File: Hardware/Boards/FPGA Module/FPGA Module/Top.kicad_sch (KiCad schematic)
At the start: 0 parts

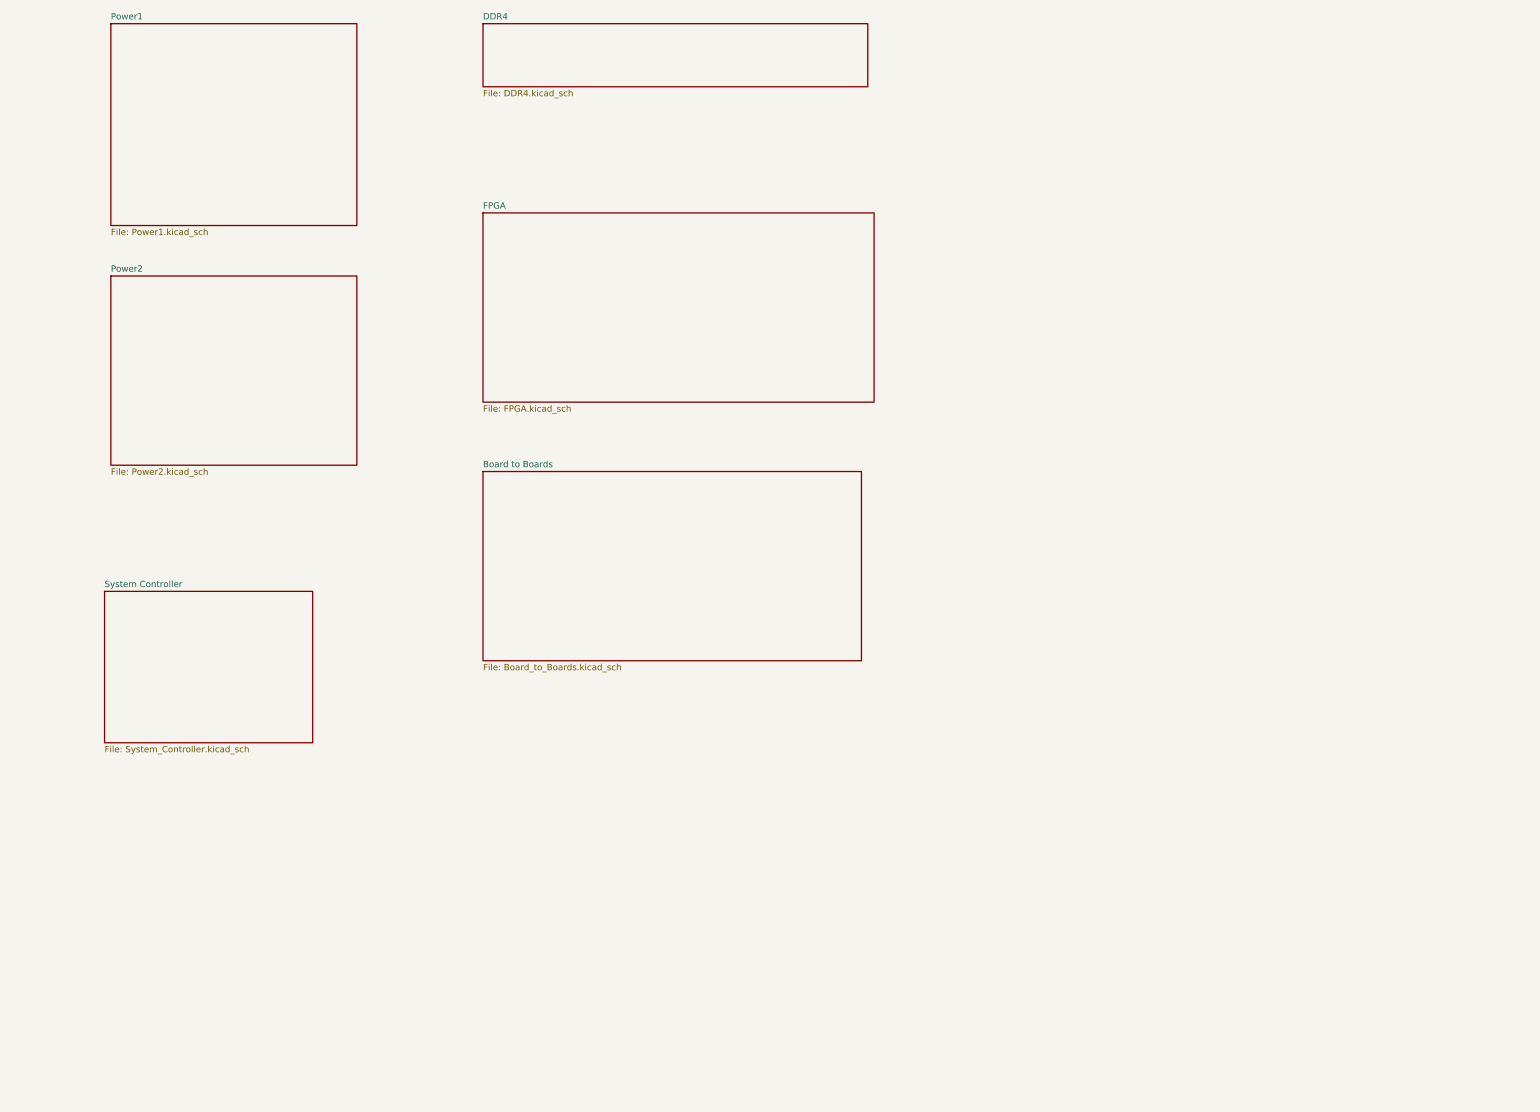
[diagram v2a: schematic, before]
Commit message: FPGA Module schematic and part edits
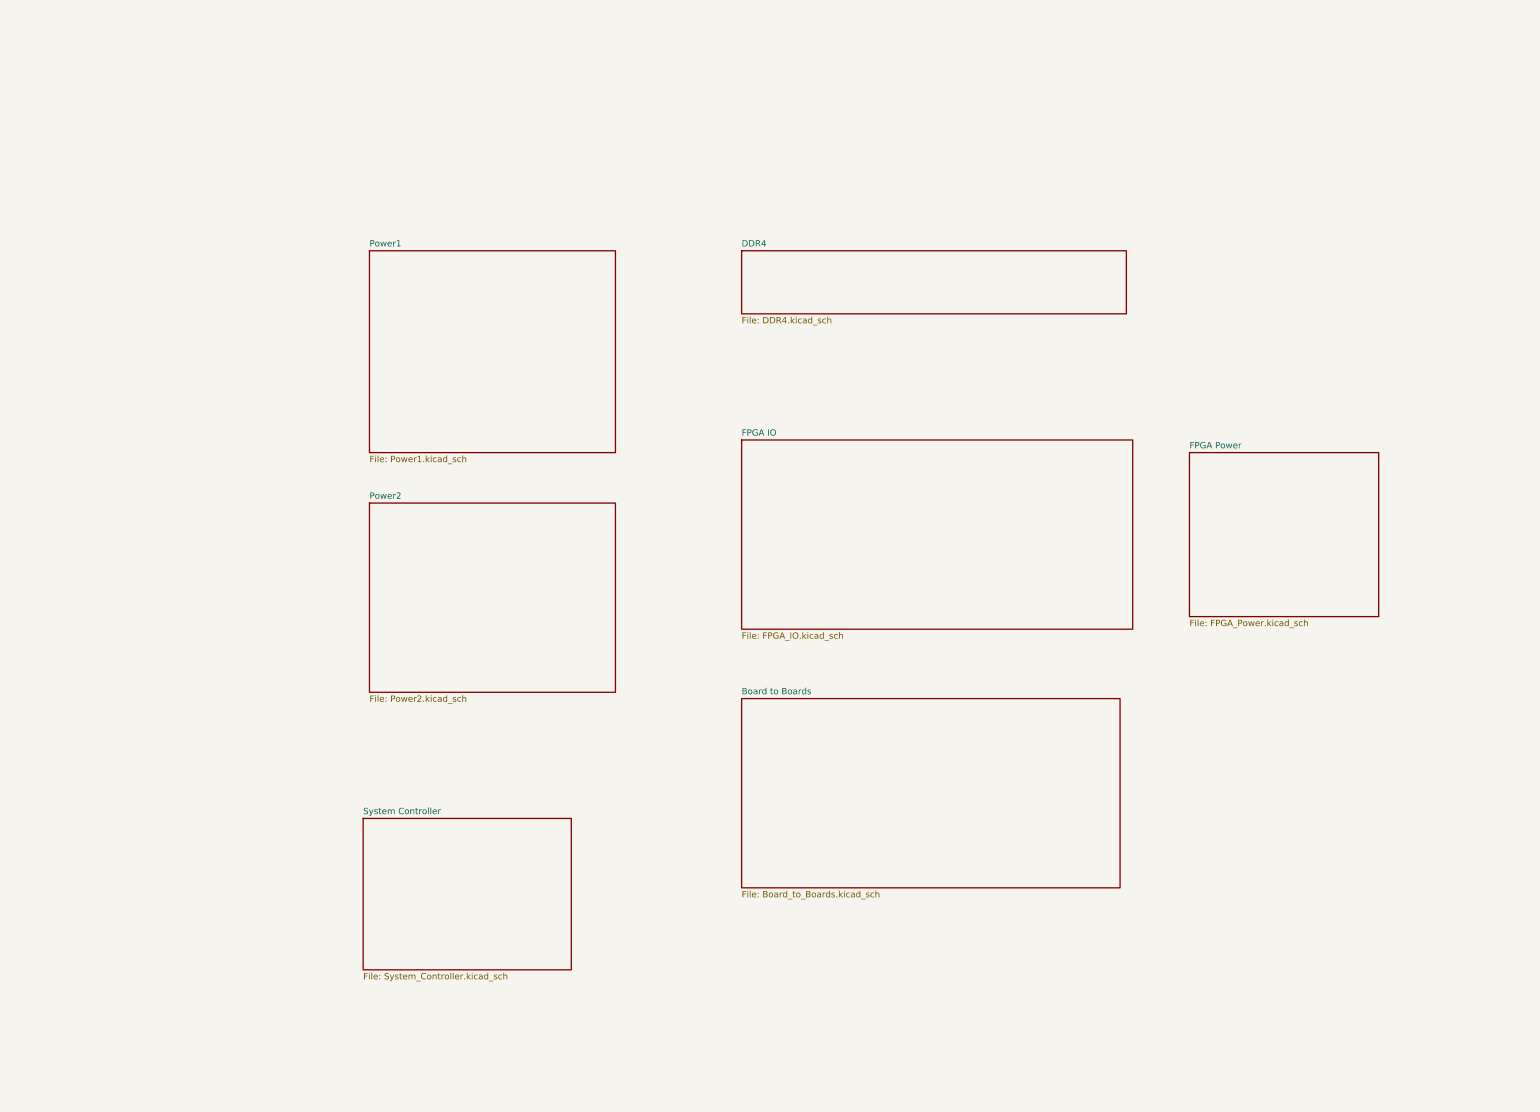
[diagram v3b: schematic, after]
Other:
- sheet FPGA renamed FPGA IO
- added sheet FPGA Power (FPGA_Power.kicad_sch)
- sheet FPGA IO: file FPGA.kicad_sch -> FPGA_IO.kicad_sch
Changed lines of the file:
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@@
 	(generator "eeschema")
 	(generator_version "8.0")
-	(paper "A4")
+	(paper "A3")
 	(title_block
 		(title "Top")
@@
 	)
 	(sheet
-		(at 77.47 76.2)
+		(at 129.54 121.92)
 		(size 49.53 38.1)
 		(fields_autoplaced yes)
@@
 		)
 		(property "Sheetname" "Power2"
-			(at 77.47 75.4884 0)
+			(at 129.54 121.2084 0)
 			(effects
 				(font
@@
 		)
 		(property "Sheetfile" "Power2.kicad_sch"
-			(at 77.47 114.8846 0)
+			(at 129.54 160.6046 0)
+			(effects
+				(font
+					(size 1.27 1.27)
+				)
+				(justify left top)
+			)
+		)
+		(instances
+			(project "FPGA Module"
+				(path "/199f10e2-d4b4-4a27-9e84-7b1ce2ae6bf0/0c296310-f788-47f0-8a3f-43c3444563e8"
+					(page "9")
+				)
+			)
+		)
+	)
+	(sheet
+		(at 204.47 109.22)
+		(size 78.74 38.1)
+		(fields_autoplaced yes)
+		(stroke
+			(width 0.1524)
+			(type solid)
+		)
+		(fill
+			(color 0 0 0 0.0000)
+		)
+		(property "Sheetname" "FPGA IO"
+			(at 204.47 108.5084 0)
+			(effects
+				(font
+					(size 1.27 1.27)
+				)
+				(justify left bottom)
+			)
+		)
+		(property "Sheetfile" "FPGA_IO.kicad_sch"
+			(at 204.47 147.9046 0)
+			(effects
+				(font
+					(size 1.27 1.27)
+				)
+				(justify left top)
+			)
+		)
+		(instances
+			(project "FPGA Module"
+				(path "/199f10e2-d4b4-4a27-9e84-7b1ce2ae6bf0/0c296310-f788-47f0-8a3f-43c3444563e8"
+					(page "3")
+				)
+			)
+		)
+	)
+	(sheet
+		(at 204.47 71.12)
+		(size 77.47 12.7)
+		(fields_autoplaced yes)
+		(stroke
+			(width 0.1524)
+			(type solid)
+		)
+		(fill
+			(color 0 0 0 0.0000)
+		)
+		(property "Sheetname" "DDR4"
+			(at 204.47 70.4084 0)
+			(effects
+				(font
+					(size 1.27 1.27)
+				)
+				(justify left bottom)
+			)
+		)
+		(property "Sheetfile" "DDR4.kicad_sch"
+			(at 204.47 84.4046 0)
+			(effects
+				(font
+					(size 1.27 1.27)
+				)
+				(justify left top)
+			)
+		)
+		(instances
+			(project "FPGA Module"
+				(path "/199f10e2-d4b4-4a27-9e84-7b1ce2ae6bf0/0c296310-f788-47f0-8a3f-43c3444563e8"
+					(page "5")
+				)
+			)
+		)
+	)
+	(sheet
+		(at 128.27 185.42)
+		(size 41.91 30.48)
+		(fields_autoplaced yes)
+		(stroke
+			(width 0.1524)
+			(type solid)
+		)
+		(fill
+			(color 0 0 0 0.0000)
+		)
+		(property "Sheetname" "System Controller"
+			(at 128.27 184.7084 0)
+			(effects
+				(font
+					(size 1.27 1.27)
+				)
+				(justify left bottom)
+			)
+		)
+		(property "Sheetfile" "System_Controller.kicad_sch"
+			(at 128.27 216.4846 0)
+			(effects
+				(font
+					(size 1.27 1.27)
+				)
+				(justify left top)
+			)
+		)
+		(instances
+			(project "FPGA Module"
+				(path "/199f10e2-d4b4-4a27-9e84-7b1ce2ae6bf0/0c296310-f788-47f0-8a3f-43c3444563e8"
+					(page "6")
+				)
+			)
+		)
+	)
+	(sheet
+		(at 129.54 71.12)
+		(size 49.53 40.64)
+		(fields_autoplaced yes)
+		(stroke
+			(width 0.1524)
+			(type solid)
+		)
+		(fill
+			(color 0 0 0 0.0000)
+		)
+		(property "Sheetname" "Power1"
+			(at 129.54 70.4084 0)
+			(effects
+				(font
+					(size 1.27 1.27)
+				)
+				(justify left bottom)
+			)
+		)
+		(property "Sheetfile" "Power1.kicad_sch"
+			(at 129.54 112.3446 0)
 			(effects
 				(font
@@
 	)
 	(sheet
-		(at 152.4 63.5)
-		(size 78.74 38.1)
-		(fields_autoplaced yes)
-		(stroke
-			(width 0.1524)
-			(type solid)
-		)
-		(fill
-			(color 0 0 0 0.0000)
-		)
-		(property "Sheetname" "FPGA"
-			(at 152.4 62.7884 0)
-			(effects
-				(font
-					(size 1.27 1.27)
-				)
-				(justify left bottom)
-			)
-		)
-		(property "Sheetfile" "FPGA.kicad_sch"
-			(at 152.4 102.1846 0)
-			(effects
-				(font
-					(size 1.27 1.27)
-				)
-				(justify left top)
-			)
-		)
-		(instances
-			(project "FPGA Module"
-				(path "/199f10e2-d4b4-4a27-9e84-7b1ce2ae6bf0/0c296310-f788-47f0-8a3f-43c3444563e8"
-					(page "3")
-				)
-			)
-		)
-	)
-	(sheet
-		(at 152.4 25.4)
-		(size 77.47 12.7)
-		(fields_autoplaced yes)
-		(stroke
-			(width 0.1524)
-			(type solid)
-		)
-		(fill
-			(color 0 0 0 0.0000)
-		)
-		(property "Sheetname" "DDR4"
-			(at 152.4 24.6884 0)
-			(effects
-				(font
-					(size 1.27 1.27)
-				)
-				(justify left bottom)
-			)
-		)
-		(property "Sheetfile" "DDR4.kicad_sch"
-			(at 152.4 38.6846 0)
+		(at 204.47 161.29)
+		(size 76.2 38.1)
+		(fields_autoplaced yes)
+		(stroke
+			(width 0.1524)
+			(type solid)
+		)
+		(fill
+			(color 0 0 0 0.0000)
+		)
+		(property "Sheetname" "Board to Boards"
+			(at 204.47 160.5784 0)
+			(effects
+				(font
+					(size 1.27 1.27)
+				)
+				(justify left bottom)
+			)
+		)
+		(property "Sheetfile" "Board_to_Boards.kicad_sch"
+			(at 204.47 199.9746 0)
+			(effects
+				(font
+					(size 1.27 1.27)
+				)
+				(justify left top)
+			)
+		)
+		(instances
+			(project "FPGA Module"
+				(path "/199f10e2-d4b4-4a27-9e84-7b1ce2ae6bf0/0c296310-f788-47f0-8a3f-43c3444563e8"
+					(page "7")
+				)
+			)
+		)
+	)
+	(sheet
+		(at 294.64 111.76)
+		(size 38.1 33.02)
+		(fields_autoplaced yes)
+		(stroke
+			(width 0.1524)
+			(type solid)
+		)
+		(fill
+			(color 0 0 0 0.0000)
+		)
+		(property "Sheetname" "FPGA Power"
+			(at 294.64 111.0484 0)
+			(effects
+				(font
+					(size 1.27 1.27)
+				)
+				(justify left bottom)
+			)
+		)
+		(property "Sheetfile" "FPGA_Power.kicad_sch"
+			(at 294.64 145.3646 0)
 			(effects
 				(font
@@
 				)
 			)
-		)
-	)
-	(sheet
-		(at 76.2 139.7)
-		(size 41.91 30.48)
-		(fields_autoplaced yes)
-		(stroke
-			(width 0.1524)
-			(type solid)
-		)
-		(fill
-			(color 0 0 0 0.0000)
-		)
-		(property "Sheetname" "System Controller"
-			(at 76.2 138.9884 0)
-			(effects
-				(font
-					(size 1.27 1.27)
-				)
-				(justify left bottom)
-			)
-		)
-		(property "Sheetfile" "System_Controller.kicad_sch"
-			(at 76.2 170.7646 0)
-			(effects
-				(font
-					(size 1.27 1.27)
-				)
-				(justify left top)
-			)
-		)
-		(instances
-			(project "FPGA Module"
-				(path "/199f10e2-d4b4-4a27-9e84-7b1ce2ae6bf0/0c296310-f788-47f0-8a3f-43c3444563e8"
-					(page "5")
-				)
-			)
-		)
-	)
-	(sheet
-		(at 77.47 25.4)
-		(size 49.53 40.64)
-		(fields_autoplaced yes)
-		(stroke
-			(width 0.1524)
-			(type solid)
-		)
-		(fill
-			(color 0 0 0 0.0000)
-		)
-		(property "Sheetname" "Power1"
-			(at 77.47 24.6884 0)
-			(effects
-				(font
-					(size 1.27 1.27)
-				)
-				(justify left bottom)
-			)
-		)
-		(property "Sheetfile" "Power1.kicad_sch"
-			(at 77.47 66.6246 0)
-			(effects
-				(font
-					(size 1.27 1.27)
-				)
-				(justify left top)
-			)
-		)
-		(instances
-			(project "FPGA Module"
-				(path "/199f10e2-d4b4-4a27-9e84-7b1ce2ae6bf0/0c296310-f788-47f0-8a3f-43c3444563e8"
-					(page "7")
-				)
-			)
-		)
-	)
-	(sheet
-		(at 152.4 115.57)
-		(size 76.2 38.1)
-		(fields_autoplaced yes)
-		(stroke
-			(width 0.1524)
-			(type solid)
-		)
-		(fill
-			(color 0 0 0 0.0000)
-		)
-		(property "Sheetname" "Board to Boards"
-			(at 152.4 114.8584 0)
-			(effects
-				(font
-					(size 1.27 1.27)
-				)
-				(justify left bottom)
-			)
-		)
-		(property "Sheetfile" "Board_to_Boards.kicad_sch"
-			(at 152.4 154.2546 0)
-			(effects
-				(font
-					(size 1.27 1.27)
-				)
-				(justify left top)
-			)
-		)
-		(instances
-			(project "FPGA Module"
-				(path "/199f10e2-d4b4-4a27-9e84-7b1ce2ae6bf0/0c296310-f788-47f0-8a3f-43c3444563e8"
-					(page "6")
-				)
-			)

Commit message: Added FPGA Config page
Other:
- added sheet FPGA Config (FPGA Config.kicad_sch)
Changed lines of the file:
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@@
+	)
+	(sheet
+		(at 81.915 79.375)
+		(size 31.115 48.895)
+		(fields_autoplaced yes)
+		(stroke
+			(width 0.1524)
+			(type solid)
+		)
+		(fill
+			(color 0 0 0 0.0000)
+		)
+		(property "Sheetname" "FPGA Config"
+			(at 81.915 78.6634 0)
+			(effects
+				(font
+					(size 1.27 1.27)
+				)
+				(justify left bottom)
+			)
+		)
+		(property "Sheetfile" "FPGA Config.kicad_sch"
+			(at 81.915 128.8546 0)
+			(effects
+				(font
+					(size 1.27 1.27)
+				)
+				(justify left top)
+			)
+		)
+		(instances
+			(project "FPGA Module"
+				(path "/199f10e2-d4b4-4a27-9e84-7b1ce2ae6bf0/0c296310-f788-47f0-8a3f-43c3444563e8"
+					(page "10")
+				)
+			)
+		)
 	)
 	(sheet

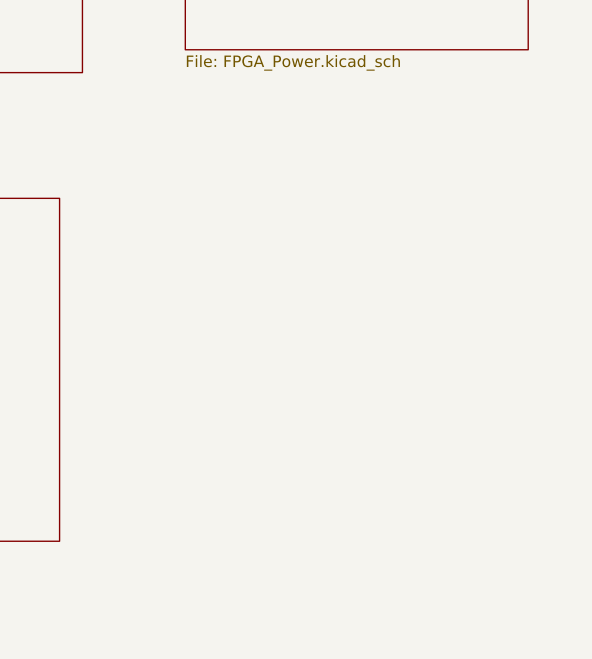
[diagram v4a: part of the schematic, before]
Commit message: Using new DP to HDMI IC
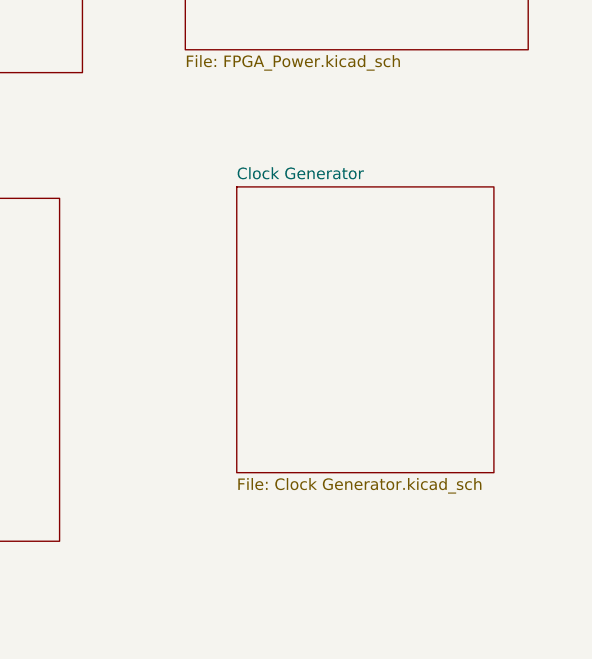
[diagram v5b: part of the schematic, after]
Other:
- added sheet Clock Generator (Clock Generator.kicad_sch)
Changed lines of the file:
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@@
+	)
+	(sheet
+		(at 300.355 160.02)
+		(size 28.575 31.75)
+		(fields_autoplaced yes)
+		(stroke
+			(width 0.1524)
+			(type solid)
+		)
+		(fill
+			(color 0 0 0 0.0000)
+		)
+		(property "Sheetname" "Clock Generator"
+			(at 300.355 159.3084 0)
+			(effects
+				(font
+					(size 1.27 1.27)
+				)
+				(justify left bottom)
+			)
+		)
+		(property "Sheetfile" "Clock Generator.kicad_sch"
+			(at 300.355 192.3546 0)
+			(effects
+				(font
+					(size 1.27 1.27)
+				)
+				(justify left top)
+			)
+		)
+		(instances
+			(project "FPGA Module"
+				(path "/199f10e2-d4b4-4a27-9e84-7b1ce2ae6bf0/0c296310-f788-47f0-8a3f-43c3444563e8"
+					(page "11")
+				)
+			)
+		)
 	)
 	(sheet
